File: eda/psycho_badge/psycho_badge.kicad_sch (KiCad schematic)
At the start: 0 parts

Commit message: added eink display circuit and dev board
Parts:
- added C10, C11, C12, C2, C5, C6, C7, C9: 1uF, 0_local:C_0805_2012Metric, symbol 0_local:C_0805
- added C3, C4: 4.7uF, 0_local:C_0805_2012Metric, symbol 0_local:C_0805
- added D1, D2, D3: MBR0530, 0_local:D_SOD-123, symbol 0_local:D_MBR0530
- added FPC1: FPC05-H0.5-24AH2.0, 0_local:FPC-SMD_24P-P0.50_FPC05-H0.5-24AH2.0, symbol 0_local:FPC05-H0.5-24AH2.0_GDEM_EINK
- added J1: Conn_01x08, 0_local:Conn_Pin_Header_Straight_1x08_Pitch2.54mm, symbol 0_local:Conn_01x08
- added L1: 47uH, 0_local:L_APV_ANR3015, symbol 0_local:L_APV_ANR3015
- added Q1: Si1308EDL, 0_local:SOT-323_SC-70, symbol 0_local:Q_Si1308EDL_MOSFET_SOT323
- added R1: 1M, 0_local:R_0805_2012Metric, symbol 0_local:R_0805
- added R2: 2.2, 0_local:R_0805_2012Metric, symbol 0_local:R_0805
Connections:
- new net: C3.2, D1.1 (K), D2.2 (A)
- new net: C7.2, FPC1.18
- new net: C9.2, FPC1.20
- new net: C10.2, FPC1.22
- new net: C12.2, FPC1.24
- new net: C2.2, FPC1.5
- new net: C3.1, D3.2 (A), L1.2, Q1.3 (D)
- new net +3.3V: C4.2, C6.2, FPC1.15, FPC1.16, J1.1 (Pin_1), L1.1
- new net F_BUSY: FPC1.9, J1.8 (Pin_8)
- new net F_CS: FPC1.12, J1.5 (Pin_5)
- new net F_DC: FPC1.11, J1.6 (Pin_6)
- new net F_GDR: FPC1.2, Q1.1 (G), R1.1
- new net F_PREVGH: C5.2, D3.1 (K), FPC1.21
- new net F_PREVGL: C11.2, D1.2 (A), FPC1.23
- new net F_RES: FPC1.10, J1.7 (Pin_7)
- new net F_RESE: FPC1.3, Q1.2 (S), R2.1
- new net F_SCLK: FPC1.13, J1.4 (Pin_4)
- new net F_SDI: FPC1.14, J1.3 (Pin_3)
- new net GND: C10.1, C11.1, C12.1, C2.1, C4.1, C5.1, C6.1, C7.1, C9.1, D2.1 (K), FPC1.17, FPC1.6, FPC1.7, FPC1.8, J1.2 (Pin_2), R1.2, R2.2
- no-connect marks 0 -> 2

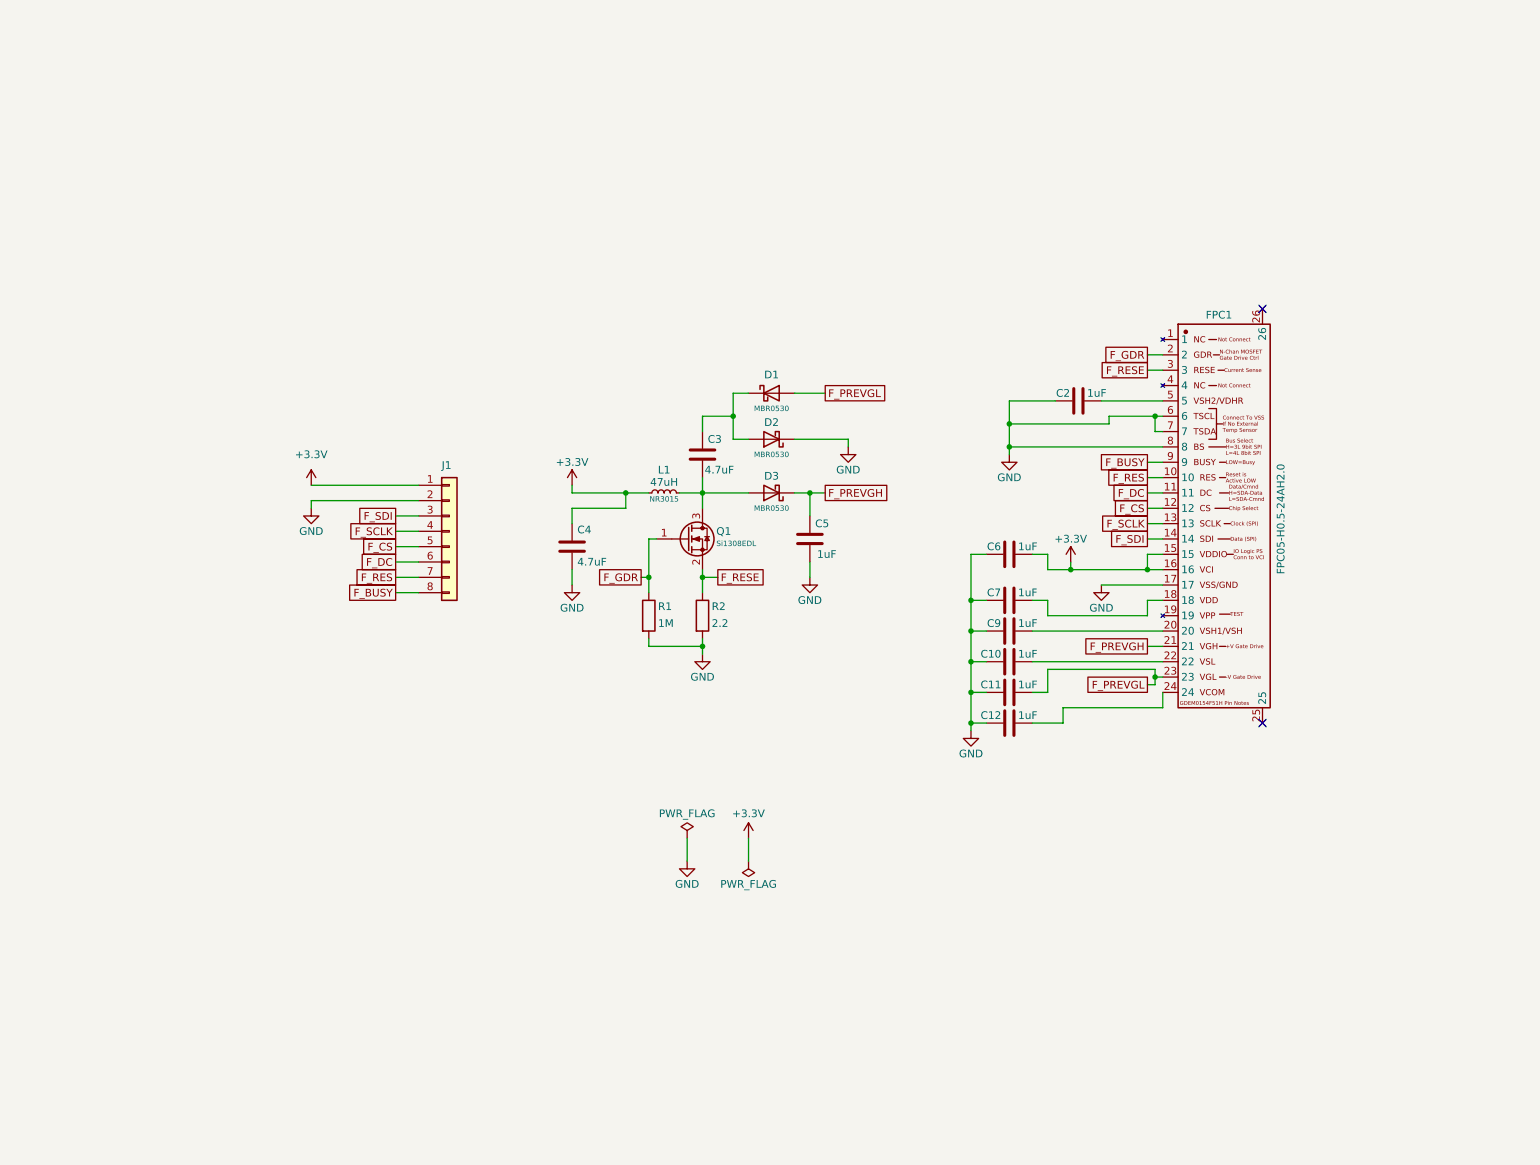
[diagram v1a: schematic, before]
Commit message: component layout done
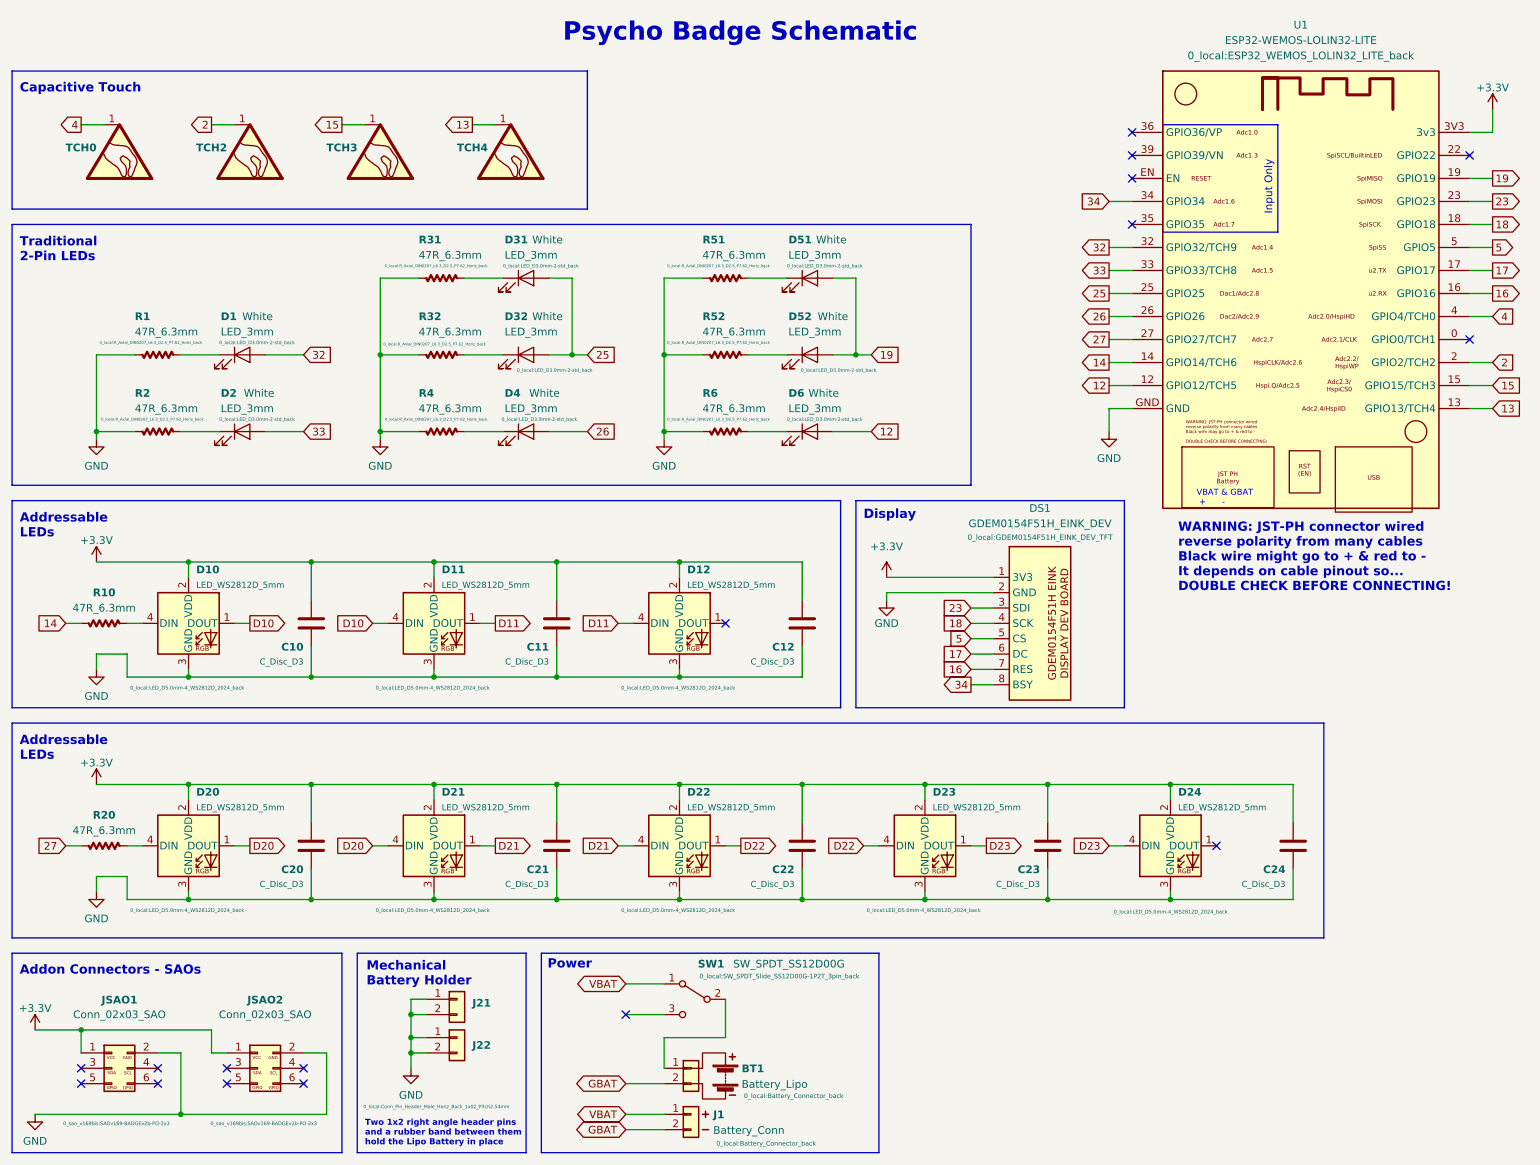
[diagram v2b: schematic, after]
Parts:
- removed C10, C11, C12, C2, C5, C6, C7, C9: 1uF, 0_local:C_0805_2012Metric, symbol 0_local:C_0805
- removed C3, C4: 4.7uF, 0_local:C_0805_2012Metric, symbol 0_local:C_0805
- removed D1, D2, D3: MBR0530, 0_local:D_SOD-123, symbol 0_local:D_MBR0530
- removed FPC1: FPC05-H0.5-24AH2.0, 0_local:FPC-SMD_24P-P0.50_FPC05-H0.5-24AH2.0, symbol 0_local:FPC05-H0.5-24AH2.0_GDEM_EINK
- removed J1: Conn_01x08, 0_local:Conn_Pin_Header_Straight_1x08_Pitch2.54mm, symbol 0_local:Conn_01x08
- removed L1: 47uH, 0_local:L_APV_ANR3015, symbol 0_local:L_APV_ANR3015
- removed Q1: Si1308EDL, 0_local:SOT-323_SC-70, symbol 0_local:Q_Si1308EDL_MOSFET_SOT323
- removed R1: 1M, 0_local:R_0805_2012Metric, symbol 0_local:R_0805
- removed R2: 2.2, 0_local:R_0805_2012Metric, symbol 0_local:R_0805
- added BT1: Battery_Lipo, 0_local:Battery_Connector_back, symbol 0_local:Battery_Lipo
- added C10, C11, C12, C20, C21, C22, C23, C24: C_Disc_D3, 0_local:C_Disc_D3_back, symbol 0_local:C_Disc_D3
- added D1, D2, D31, D32, D4, D51, D52, D6: LED_3mm, 0_local:LED_D3.0mm-2-std_back, symbol 0_local:LED_THT_3mm
- added D10, D11, D12, D20, D21, D22, D23, D24: LED_WS2812D_5mm, 0_local:LED_D5.0mm-4_WS2812D_2024_back, symbol 0_local:LED_WS2812D_THT_5mm
- added DS1: GDEM0154F51H_EINK_DEV, 0_local:GDEM0154F51H_EINK_DEV_TFT, symbol 0_local:GDEM0154F51H_EINK_DEV
- added J1: Battery_Conn, 0_local:Battery_Connector_back, symbol 0_local:Battery_Conn
- added J21, J22: 01x02, 0_local:Conn_Pin_Header_Male_Horiz_Back_1x02_Pitch2.54mm, symbol 0_local:Conn_01x02
- added JSAO1, JSAO2: Conn_02x03_SAO, 0_sao_v169bis:SAOv169-BADGEv2b-PO-2x3, symbol 0_local:Conn_02x03_SAO
- added R1, R10, R2, R20, R31, R32, R4, R51, R52, R6: 47R_6.3mm, 0_local:R_Axial_DIN0207_L6.3_D2.5_P7.62_Horiz_back, symbol 0_local:R_Axial_Z_L6.3
- added SW1: SW_SPDT_SS12D00G, 0_local:SW_SPDT_Slide_SS12D00G-1P2T_3pin_back, symbol 0_local:SW_SPDT_SS12D00G
- added TCH0, TCH2, TCH3, TCH4: SYM_Touch_lg, symbol 0_local:SYM_Touch_lg
- added U1: ESP32-WEMOS-LOLIN32-LITE, 0_local:ESP32_WEMOS_LOLIN32_LITE_back, symbol 0_local:ESP32-WEMOS-LOLIN32-LITE
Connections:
- net +3.3V: now also C10.1, C11.1, C12.1, C20.1, C21.1, C22.1, C23.1, C24.1, D10.2 (VDD), D11.2 (VDD), D12.2 (VDD), D20.2 (VDD), D21.2 (VDD), D22.2 (VDD), D23.2 (VDD), D24.2 (VDD), DS1.1 (3V3), JSAO1.1 (Pin_1), JSAO2.1 (Pin_1), U1.3V3 (3v3)
- net GND: now also C10.2, C11.2, C12.2, C20.2, C21.2, C22.2, C23.2, C24.2, D10.3 (GND), D11.3 (GND), D12.3 (GND), D20.3 (GND), D21.3 (GND), D22.3 (GND), D23.3 (GND), D24.3 (GND), DS1.2 (GND), J21.1 (Pin_1), J21.2 (Pin_2), J22.1 (Pin_1), J22.2 (Pin_2), JSAO1.2 (Pin_2), JSAO2.2 (Pin_2), R1.2, R2.2, R31.2, R32.2, R4.2, R51.2, R52.2, R6.2, U1.GND
- new net: D20.4 (DIN), R20.1
- new net: D51.1 (K), R51.1
- new net: D6.1 (K), R6.1
- new net: D1.1 (K), R1.1
- new net: D10.4 (DIN), R10.1
- new net: BT1.1 (Pin_1), SW1.2 (B)
- new net: D2.1 (K), R2.1
- new net: D31.1 (K), R31.1
- new net: D52.1 (K), R52.1
- new net: D4.1 (K), R4.1
- new net: D32.1 (K), R32.1
- new net 12: D6.2 (A), U1.12 (GPIO12/TCH5)
- new net 13: TCH4.1, U1.13 (GPIO13/TCH4)
- new net 14: R10.2, U1.14 (GPIO14/TCH6)
- new net 15: TCH3.1, U1.15 (GPIO15/TCH3)
- new net 16: DS1.7 (RES), U1.16 (GPIO16)
- new net 17: DS1.6 (DC), U1.17 (GPIO17)
- new net 18: DS1.4 (SCK), U1.18 (GPIO18)
- new net 19: D51.2 (A), D52.2 (A), U1.19 (GPIO19)
- new net 2: TCH2.1, U1.2 (GPIO2/TCH2)
- new net 23: DS1.3 (SDI), U1.23 (GPIO23)
- new net 25: D31.2 (A), D32.2 (A), U1.25 (GPIO25)
- new net 26: D4.2 (A), U1.26 (GPIO26)
- new net 27: R20.2, U1.27 (GPIO27/TCH7)
- new net 32: D1.2 (A), U1.32 (GPIO32/TCH9)
- new net 33: D2.2 (A), U1.33 (GPIO33/TCH8)
- new net 34: DS1.8 (BSY), U1.34 (GPIO34)
- new net 4: TCH0.1, U1.4 (GPIO4/TCH0)
- new net 5: DS1.5 (CS), U1.5 (GPIO5)
- new net D10: D10.1 (DOUT), D11.4 (DIN)
- new net D11: D11.1 (DOUT), D12.4 (DIN)
- new net D20: D20.1 (DOUT), D21.4 (DIN)
- new net D21: D21.1 (DOUT), D22.4 (DIN)
- new net D22: D22.1 (DOUT), D23.4 (DIN)
- new net D23: D23.1 (DOUT), D24.4 (DIN)
- new net GBAT: BT1.2 (Pin_2), J1.2 (Pin_2)
- new net VBAT: J1.1 (Pin_1), SW1.1 (A)
- no-connect marks 2 -> 17
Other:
- note added: "Addon Connectors - SAOs"
- note added: "Addressable LEDs"
- note added: "Capacitive Touch"
- note added: "Display"
- note added: "Input Only"
- note added: "Mechanical Battery Holder"
- note added: "Power"
- note added: "Psycho Badge Schematic"
- note added: "Traditional 2-Pin LEDs"
- note added: "Two 1x2 right angle header pins and a rubber band between them hold the Lipo Battery in place"
- note added: "VBAT & GBAT + -"
- note added: "WARNING: JST-PH connector wired reverse polarity from many cables Black wire might go to + & red to - It depends on cable pinout so... DOUBLE CHECK BEFORE CONNECTING!"

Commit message: main pcb complete
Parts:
- removed TCH0, TCH2, TCH3, TCH4: SYM_Touch_lg, symbol 0_local:SYM_Touch_lg
- added TCH1: SYM_Touch_lg_x4, 0_badge:psycho_badge_top_art_fcu, symbol 0_local:SYM_Touch_lg_x4
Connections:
- net 13: now also TCH1.4
- net 14: now also R20.2; no longer R10.2
- net 15: now also TCH1.3
- net 2: now also TCH1.2
- net 25: now also D4.2 (A); no longer D31.2 (A), D32.2 (A)
- net 26: now also D31.2 (A), D32.2 (A); no longer D4.2 (A)
- net 27: now also R10.2; no longer R20.2
- net 32: now also D2.2 (A); no longer D1.2 (A)
- net 33: now also D1.2 (A); no longer D2.2 (A)
- net 4: now also TCH1.1
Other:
- note added: "This represents four differnt capacitive touch zones in a single footprint"
